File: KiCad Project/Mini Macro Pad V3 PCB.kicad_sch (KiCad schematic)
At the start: 55 parts, among them J1 USB_C_Receptacle_USB2.0_14P, SW1 SW_Push bootsel, SW10 SW_Push, SW11 SW_Push, SW12 SW_Push, SW13 SW_Push, SW14 SW_Push, SW15 SW_Push, SW16 SW_Push, SW17 SW_Push, SW18 SW_Push, SW19 SW_Push, SW2 SW_Push, SW20 SW_Push, SW21 SW_Push, SW22 RotaryEncoder_Switch_MP, SW23 RotaryEncoder_Switch_MP, SW3 SW_Push, SW4 SW_Push, SW5 SW_Push, SW6 SW_Push, SW7 SW_Push, SW8 SW_Push, SW9 SW_Push, U1 RP2040, U2 NCP1117-3.3_SOT223, U3 W25Q128JVS, Y1 ABM8-272-T3

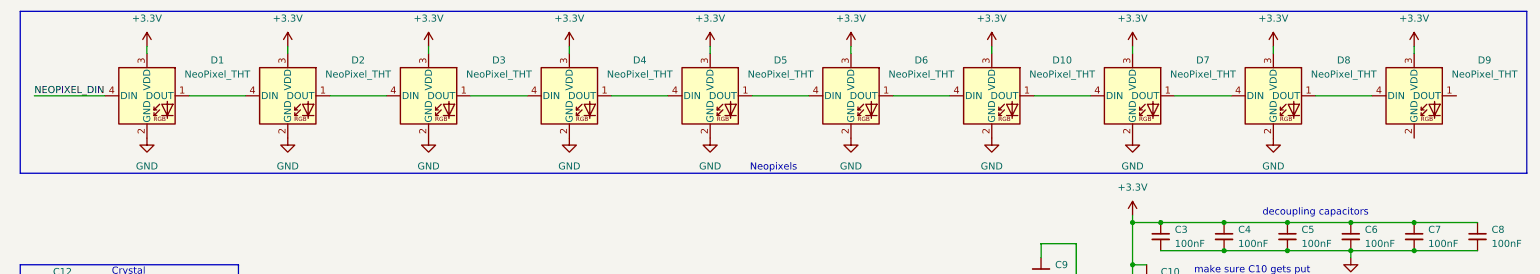
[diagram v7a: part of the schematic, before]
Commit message: assigned footprints to neopixels
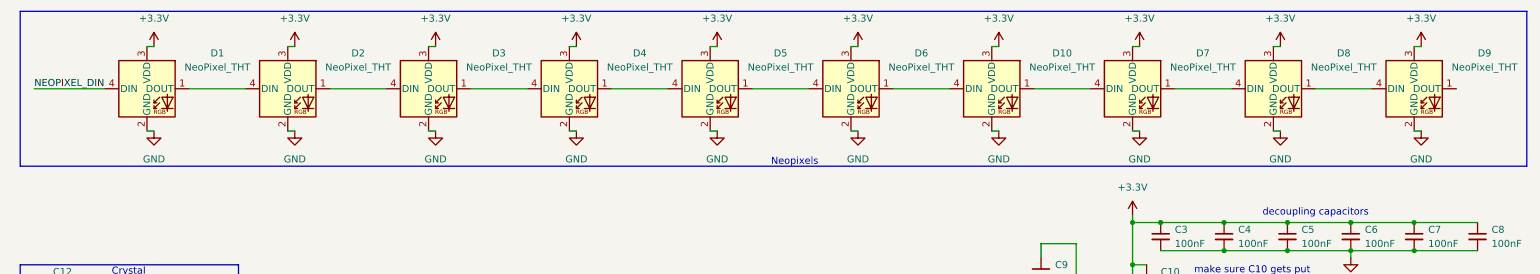
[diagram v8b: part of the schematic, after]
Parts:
- D1, D10, D2, D3, D4, D5, D6, D7, D8, D9: footprint (none) -> LED_SMD:LED_SK6812_PLCC4_5.0x5.0mm_P3.2mm
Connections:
- net GND: now also D9.2 (GND)
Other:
- moved on the sheet: D1, D10, D2, D3, D4, D5, D6, D7, D8, D9
